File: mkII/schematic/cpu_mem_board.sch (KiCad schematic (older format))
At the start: 28 parts, among them J1 Conn_01x37_Male, Q1 2N2219, Q2 BC108, Q3 2N2219, SW1 SW_SPDT, U1 Z80CPU, U2 KM62256CLP, U3 27128, U4 KM62256CLP, U5 74LS156

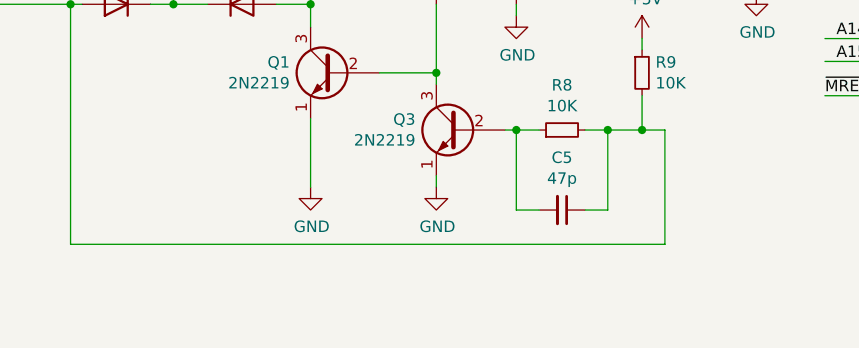
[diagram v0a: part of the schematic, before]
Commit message: Add note to CPU schematic.
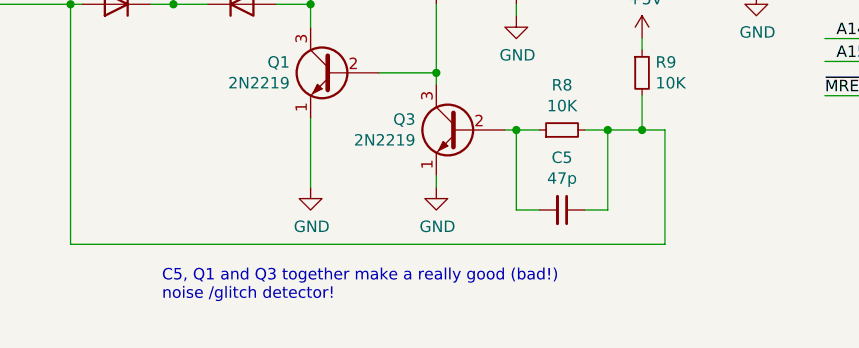
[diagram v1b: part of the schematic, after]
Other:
- note added: "C5, Q1 and Q3 together make a really good (bad!)\nnoise /glitch detector!"
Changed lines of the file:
@@
 Wire Bus Line
 	4050 800  4050 3150
+Text Notes 5350 6200 0    50   ~ 0
+C5, Q1 and Q3 together make a really good (bad!)\nnoise /glitch detector!
 $EndSCHEMATC
